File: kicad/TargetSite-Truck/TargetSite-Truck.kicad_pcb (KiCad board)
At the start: 2 copper layers, 75 x 50 mm, 11 parts, among them J2 HC05, M1 Motor_DC, U1 PIC16F1827-E/P, U2 TA7291P

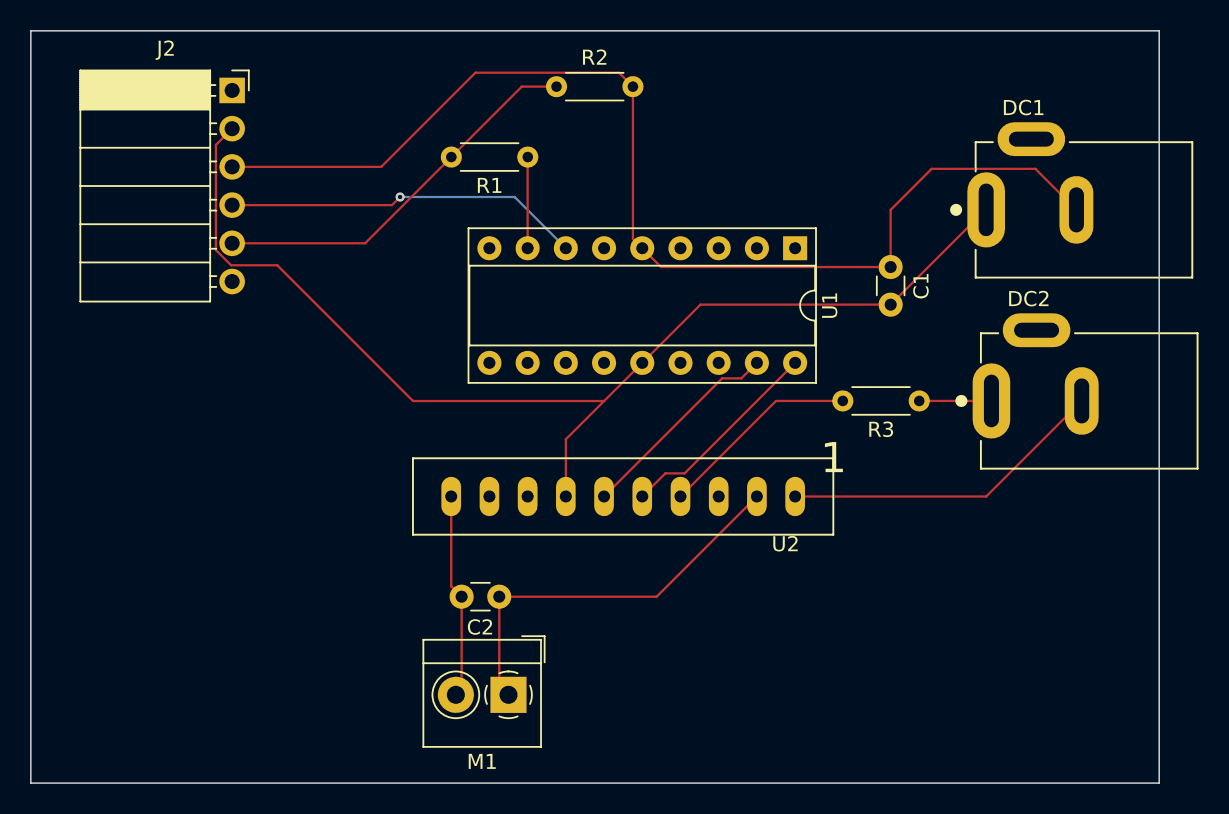
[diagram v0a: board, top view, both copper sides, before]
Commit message: 回路図の作成、PCBの作成
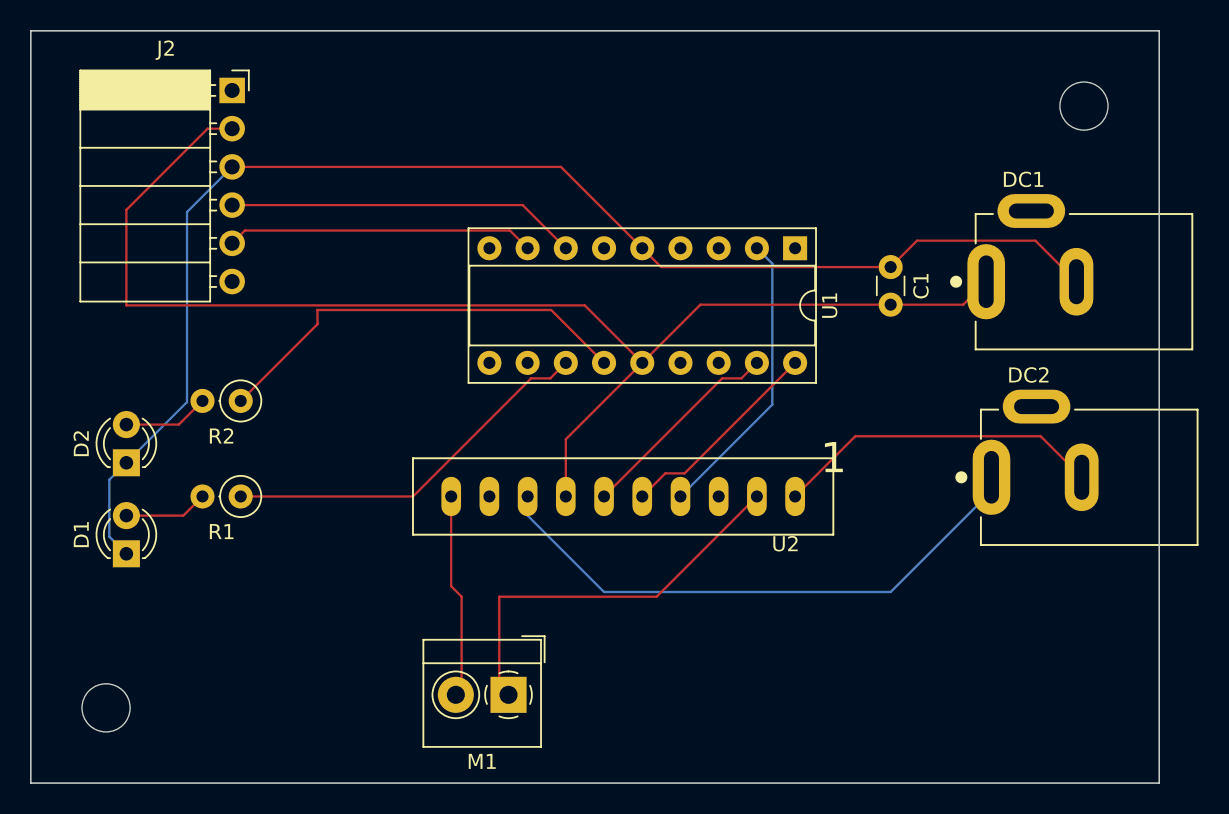
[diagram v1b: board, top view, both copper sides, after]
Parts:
- removed C2: 0.01u, Capacitor_THT:C_Disc_D3.0mm_W1.6mm_P2.50mm
- removed R3: 2.2k, Resistor_THT:R_Axial_DIN0204_L3.6mm_D1.6mm_P5.08mm_Horizontal
- added D1: LED_STATUS, LED_THT:LED_D3.0mm, F.Cu at (136.4, 114.8)
- added D2: LED_ACTIVATE, LED_THT:LED_D3.0mm, F.Cu at (136.4, 108.7)
- added MH1: MountingHole_3.2mm_M3, MountingHole:MountingHole_3.2mm_M3, F.Cu at (200.0, 85.0)
- added MH2: MountingHole_3.2mm_M3, MountingHole:MountingHole_3.2mm_M3, F.Cu at (135.0, 125.0)
- J2: value HC05 -> HM10
- R1: value 1k -> R330; footprint Resistor_THT:R_Axial_DIN0204_L3.6mm_D1.6mm_P5.08mm_Horizontal -> Resistor_THT:R_Axial_DIN0207_L6.3mm_D2.5mm_P2.54mm_Vertical
- R2: value 10k -> R330; footprint Resistor_THT:R_Axial_DIN0204_L3.6mm_D1.6mm_P5.08mm_Horizontal -> Resistor_THT:R_Axial_DIN0207_L6.3mm_D2.5mm_P2.54mm_Vertical
- moved R2 29.6 mm to (143.9, 104.6), turned to 180 degrees
- moved R1 29.5 mm to (143.9, 111.0)
- moved DC2 5.08 mm to (193.8, 109.7)
- moved DC1 4.77 mm to (193.5, 96.7)
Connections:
- net /DC_GND renamed DC_GND
- net /Driver_IN1 renamed Driver_IN1
- net /Driver_IN2 renamed Driver_IN2
- net /HC05_TX renamed HM10_TX
- net /Motor_IN1 renamed Motor_IN1
- net /Motor_IN2 renamed Motor_IN2
- DC2 pad 1: /DC_VCC -> DC_VCC
- J2 pad 5: /HC05_RX -> HM10_RX
- R1 pad 1: Net-(R1-Pad1) -> Net-(U1-Pad12)
- R1 pad 2: /HC05_RX -> Net-(D1-Pad2)
- R2 pad 1: /HC05_RX -> Net-(U1-Pad13)
- R2 pad 2: GND -> Net-(D2-Pad2)
- U1 pad 12: unconnected-(U1-Pad12) -> Net-(U1-Pad12)
- U1 pad 13: unconnected-(U1-Pad13) -> Net-(U1-Pad13)
- U1 pad 2: unconnected-(U1-Pad2) -> Driver_Ref
- U1 pad 8: Net-(R1-Pad1) -> HM10_RX
- U2 pad 4: /DC_VCC -> Driver_Ref
- U2 pad 8: /DC_VCC -> DC_VCC
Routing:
- net DC_VCC: track 0.00 -> 37.9 mm
- net Net-(U1-Pad13): track 0.00 -> 28.7 mm
- net /HC05_RX: track 25.9 -> 0.00 mm
- net Net-(U1-Pad12): track 0.00 -> 25.3 mm
- net HM10_RX: track 0.00 -> 20.5 mm
- net Driver_Ref: track 0.00 -> 19.5 mm
- net /DC_VCC: track 18.2 -> 0.00 mm
- net GND: track 76.1 -> 90.3 mm
- net VCC: track 76.5 -> 87.6 mm
- net Net-(R1-Pad1): track 6.06 -> 0.00 mm
- net Net-(D2-Pad2): track 0.00 -> 5.71 mm
- net Net-(D1-Pad2): track 0.00 -> 5.59 mm
- net HM10_TX: track 23.8 -> 23.4 mm, vias 1 -> 0

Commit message: ガーバーデータの作成
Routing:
- net GND: vias 0 -> 36
- added copper zone on B.Cu, net GND
- added copper zone on F.Cu, net GND
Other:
- board text added: "5V"
- board text added: "9V"
- board text added: "ACTIVE"
- board text added: "DC Motor"
- board text added: "GND"
- board text added: "HM-10 Pin Socket"
- board text added: "PIC16F1827"
- board text added: "RX"
- board text added: "STATUS"
- board text added: "TA7291P"
- board text added: "TX"
- board text added: "TargetSite-Front Dev:1 GTech9971 2023/05/27"
- board text added: "VCC"
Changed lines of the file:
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@@
     (grid_origin 130 130)
     (pcbplotparams
-      (layerselection 0x00010fc_ffffffff)
+      (layerselection 0x00010f0_ffffffff)
       (disableapertmacros false)
-      (usegerberextensions false)
-      (usegerberattributes true)
-      (usegerberadvancedattributes true)
-      (creategerberjobfile true)
+      (usegerberextensions true)
+      (usegerberattributes false)
+      (usegerberadvancedattributes false)
+      (creategerberjobfile false)
       (svguseinch false)
       (svgprecision 6)
       (excludeedgelayer true)
       (plotframeref false)
-      (viasonmask false)
+      (viasonmask true)
       (mode 1)
-      (useauxorigin false)
+      (useauxorigin true)
       (hpglpennumber 1)
       (hpglpenspeed 20)
@@
       (psa4output false)
       (plotreference true)
-      (plotvalue true)
+      (plotvalue false)
       (plotinvisibletext false)
       (sketchpadsonfab false)
@@
       (outputformat 1)
       (mirror false)
-      (drillshape 1)
+      (drillshape 0)
       (scaleselection 1)
       (outputdirectory "")
@@
   )
   (gr_rect locked (start 130 130) (end 205 80) (layer "Edge.Cuts") (width 0.1) (fill none))
+  (gr_text "RX" (at 145.875 94.44) (layer "F.SilkS")
+    (effects (font (size 1 1) (thickness 0.15)))
+  )
+  (gr_text "9V" (at 190.325 109.68 90) (layer "F.SilkS")
+    (effects (font (size 1 1) (thickness 0.15)))
+  )
+  (gr_text "GND" (at 145.875 89.36) (layer "F.SilkS")
+    (effects (font (size 1 1) (thickness 0.15)))
+  )
+  (gr_text "PIC16F1827" (at 184.61 98.25 90) (layer "F.SilkS")
+    (effects (font (size 1 1) (thickness 0.15)))
+  )
+  (gr_text "TargetSite-Front Dev:1\nGTech9971 2023/05/27" (at 185.245 126.825) (layer "F.SilkS")
+    (effects (font (size 1 1) (thickness 0.15)) (justify left))
+  )
+  (gr_text "VCC" (at 145.875 86.82) (layer "F.SilkS")
+    (effects (font (size 1 1) (thickness 0.15)))
+  )
+  (gr_text "TA7291P" (at 185.245 110.95 90) (layer "F.SilkS")
+    (effects (font (size 1 1) (thickness 0.15)))
+  )
+  (gr_text "ACTIVE" (at 131.905 107.14 90) (layer "F.SilkS")
+    (effects (font (size 1 1) (thickness 0.15)))
+  )
+  (gr_text "STATUS" (at 131.905 113.49 90) (layer "F.SilkS")
+    (effects (font (size 1 1) (thickness 0.15)))
+  )
+  (gr_text "DC Motor" (at 159.845 118.57) (layer "F.SilkS")
+    (effects (font (size 1 1) (thickness 0.15)))
+  )
+  (gr_text "TX" (at 145.875 91.9) (layer "F.SilkS")
+    (effects (font (size 1 1) (thickness 0.15)))
+  )
+  (gr_text "HM-10 Pin Socket" (at 138.89 99.52) (layer "F.SilkS")
+    (effects (font (size 1 1) (thickness 0.15)))
+  )
+  (gr_text "5V" (at 190.96 96.98 90) (layer "F.SilkS")
+    (effects (font (size 1 1) (thickness 0.15)))
+  )
   (segment (start 136.35 91.9) (end 136.35 98.25) (width 0.1524) (layer "F.Cu") (net 1))
   (segment (start 191.975 98.2) (end 193.5 96.675) (width 0.1524) (layer "F.Cu") (net 1))
   (segment (start 166.82 98.25) (end 170.64 102.07) (width 0.1524) (layer "F.Cu") (net 1))
-  (segment (start 165.56 107.15) (end 168.105 104.605) (width 0.1524) (layer "F.Cu") (net 1))
+  (segment (start 165.56 107.15) (end 170.64 102.07) (width 0.1524) (layer "F.Cu") (net 1))
   (segment (start 141.74715 86.50285) (end 136.35 91.9) (width 0.1524) (layer "F.Cu") (net 1))
   (segment (start 187.15 98.2) (end 191.975 98.2) (width 0.1524) (layer "F.Cu") (net 1))
-  (segment (start 168.105 104.605) (end 170.64 102.07) (width 0.1524) (layer "F.Cu") (net 1))
   (segment (start 143.38 86.50285) (end 141.74715 86.50285) (width 0.1524) (layer "F.Cu") (net 1))
   (segment (start 187.15 98.2) (end 174.51 98.2) (width 0.1524) (layer "F.Cu") (net 1))
@@
   (segment (start 170.64 94.45) (end 165.23285 89.04285) (width 0.1524) (layer "F.Cu") (net 2))
   (segment (start 196.7714 93.9464) (end 199.5 96.675) (width 0.1524) (layer "F.Cu") (net 2))
+  (via (at 150.32 84.28) (size 0.605) (drill 0.3) (layers "F.Cu" "B.Cu") (free) (net 2))
+  (via (at 194.77 124.285) (size 0.605) (drill 0.3) (layers "F.Cu" "B.Cu") (free) (net 2))
+  (via (at 183.975 119.205) (size 0.605) (drill 0.3) (layers "F.Cu" "B.Cu") (free) (net 2))
+  (via (at 149.05 119.205) (size 0.605) (drill 0.3) (layers "F.Cu" "B.Cu") (free) (net 2))
+  (via (at 157.305 103.965) (size 0.605) (drill 0.3) (layers "F.Cu" "B.Cu") (free) (net 2))
+  (via (at 144.605 119.205) (size 0.605) (drill 0.3) (layers "F.Cu" "B.Cu") (free) (net 2))
+  (via (at 190.96 90.63) (size 0.605) (drill 0.3) (layers "F.Cu" "B.Cu") (free) (net 2))
+  (via (at 166.195 119.205) (size 0.605) (drill 0.3) (layers "F.Cu" "B.Cu") (free) (net 2))
+  (via (at 150.32 89.995) (size 0.605) (drill 0.3) (layers "F.Cu" "B.Cu") (free) (net 2))
+  (via (at 150.32 96.345) (size 0.605) (drill 0.3) (layers "F.Cu" "B.Cu") (free) (net 2))
+  (via (at 153.495 124.285) (size 0.605) (drill 0.3) (layers "F.Cu" "B.Cu") (free) (net 2))
+  (via (at 150.32 103.965) (size 0.605) (drill 0.3) (layers "F.Cu" "B.Cu") (free) (net 2))
+  (via (at 181.435 104.6) (size 0.605) (drill 0.3) (layers "F.Cu" "B.Cu") (free) (net 2))
+  (via (at 168.735 107.14) (size 0.605) (drill 0.3) (layers "F.Cu" "B.Cu") (free) (net 2))
+  (via (at 183.975 124.285) (size 0.605) (drill 0.3) (layers "F.Cu" "B.Cu") (free) (net 2))
+  (via (at 175.085 124.285) (size 0.605) (drill 0.3) (layers "F.Cu" "B.Cu") (free) (net 2))
+  (via (at 164.925 90.63) (size 0.605) (drill 0.3) (layers "F.Cu" "B.Cu") (free) (net 2))
+  (via (at 149.05 124.285) (size 0.605) (drill 0.3) (layers "F.Cu" "B.Cu") (free) (net 2))
+  (via (at 164.925 104.6) (size 0.605) (drill 0.3) (layers "F.Cu" "B.Cu") (free) (net 2))
+  (via (at 194.77 119.205) (size 0.605) (drill 0.3) (layers "F.Cu" "B.Cu") (free) (net 2))
+  (via (at 190.96 104.6) (size 0.605) (drill 0.3) (layers "F.Cu" "B.Cu") (free) (net 2))
+  (via (at 166.195 124.285) (size 0.605) (drill 0.3) (layers "F.Cu" "B.Cu") (free) (net 2))
+  (via (at 164.925 84.28) (size 0.605) (drill 0.3) (layers "F.Cu" "B.Cu") (free) (net 2))
+  (via (at 178.26 90.63) (size 0.605) (drill 0.3) (layers "F.Cu" "B.Cu") (free) (net 2))
+  (via (at 157.305 96.345) (size 0.605) (drill 0.3) (layers "F.Cu" "B.Cu") (free) (net 2))
+  (via (at 177.625 96.345) (size 0.605) (drill 0.3) (layers "F.Cu" "B.Cu") (free) (net 2))
+  (via (at 178.26 84.28) (size 0.605) (drill 0.3) (layers "F.Cu" "B.Cu") (free) (net 2))
+  (via (at 175.085 119.205) (size 0.605) (drill 0.3) (layers "F.Cu" "B.Cu") (free) (net 2))
+  (via (at 136.35 103.965) (size 0.605) (drill 0.3) (layers "F.Cu" "B.Cu") (free) (net 2))
+  (via (at 136.35 119.205) (size 0.605) (drill 0.3) (layers "F.Cu" "B.Cu") (free) (net 2))
+  (via (at 162.385 107.14) (size 0.605) (drill 0.3) (layers "F.Cu" "B.Cu") (free) (net 2))
+  (via (at 171.91 104.6) (size 0.605) (drill 0.3) (layers "F.Cu" "B.Cu") (free) (net 2))
+  (via (at 161.75 96.345) (size 0.605) (drill 0.3) (layers "F.Cu" "B.Cu") (free) (net 2))
+  (via (at 144.605 124.285) (size 0.605) (drill 0.3) (layers "F.Cu" "B.Cu") (free) (net 2))
+  (via (at 153.495 119.205) (size 0.605) (drill 0.3) (layers "F.Cu" "B.Cu") (free) (net 2))
+  (via (at 190.96 84.28) (size 0.605) (drill 0.3) (layers "F.Cu" "B.Cu") (free) (net 2))
   (segment (start 136.350452 108.71) (end 135.221852 109.8386) (width 0.1524) (layer "B.Cu") (net 2))
   (segment (start 135.221852 113.6314) (end 136.350452 114.76) (width 0.1524) (layer "B.Cu") (net 2))
@@
   (segment (start 168.1 102.07) (end 164.5848 98.5548) (width 0.1524) (layer "F.Cu") (net 28))
   (segment (start 164.5848 98.5548) (end 149.05 98.5548) (width 0.1524) (layer "F.Cu") (net 28))
+  (zone (net 2) (net_name "GND") (layers F&B.Cu) (hatch edge 0.508)
+    (connect_pads (clearance 0.35))
+    (min_thickness 0.254) (filled_areas_thickness no)
+    (fill yes (thermal_gap 0.508) (thermal_bridge_width 0.508))
+    (polygon
+      (pts
+        (xy 204.5 129.5)
+        (xy 130.5 129.5)
+        (xy 130.5 80.5)
+        (xy 204.5 80.5)
+      )
+    )
+  )
 )

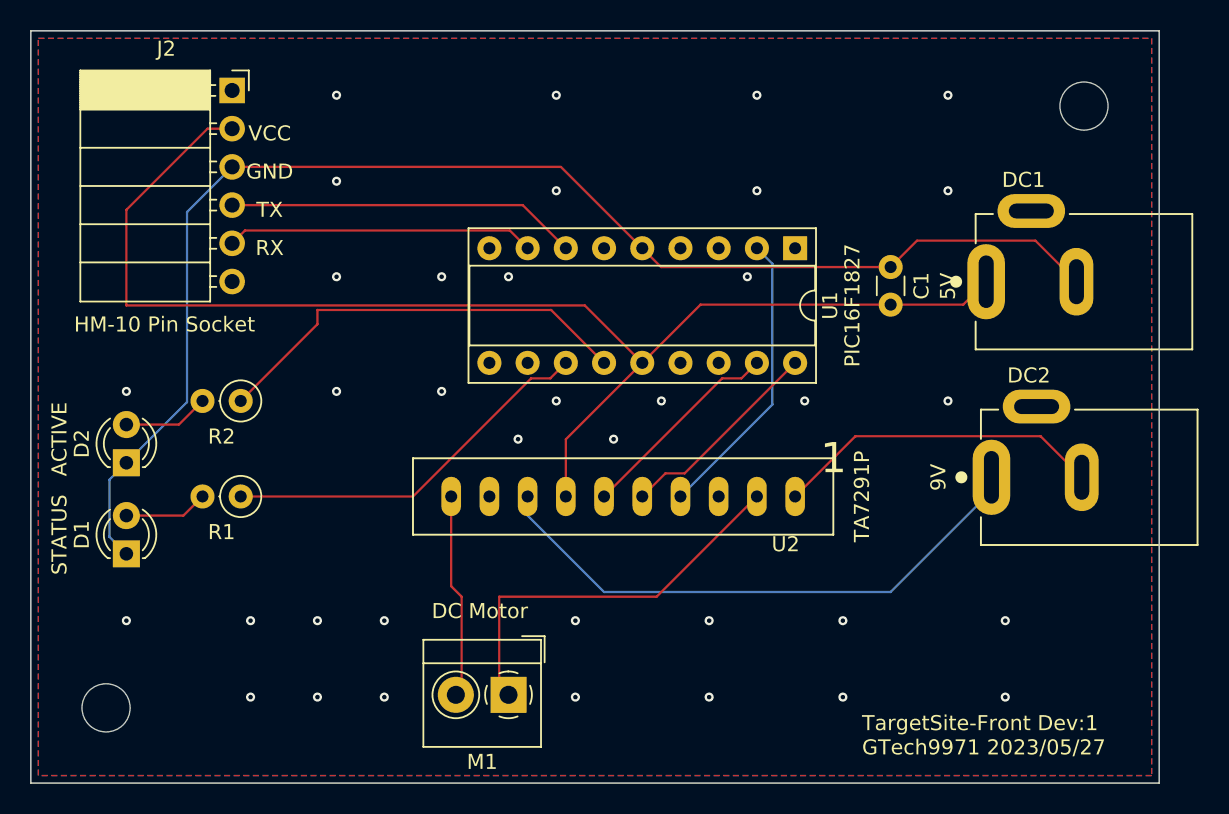
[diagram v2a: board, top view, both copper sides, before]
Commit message: 回路基板設計修正
RA0、RA1の配線を引き直した
ターミナルのピッチサイズを5.08mmに変更
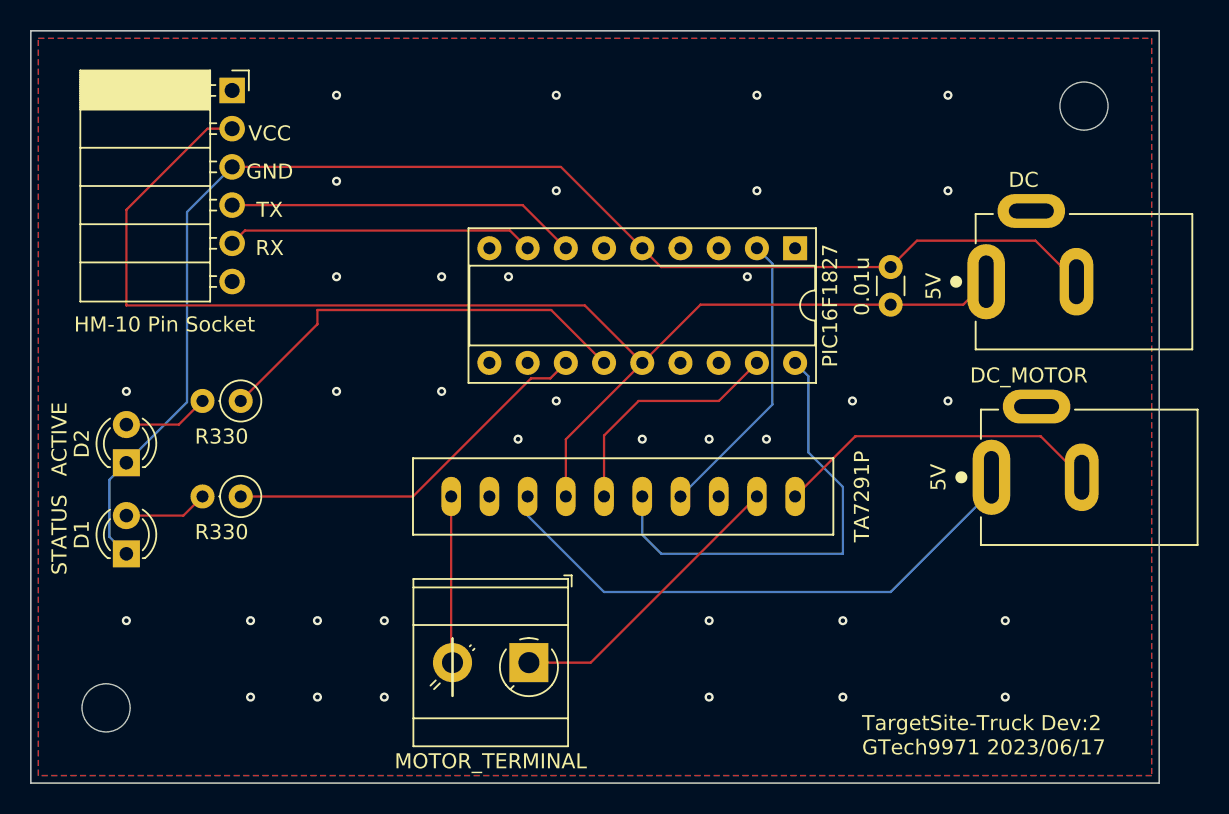
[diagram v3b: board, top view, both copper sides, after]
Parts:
- HM-10 Pin Socket: renamed from J2
- MOTOR_TERMINAL: renamed from M1; footprint TerminalBlock_4Ucon:TerminalBlock_4Ucon_1x02_P3.50mm_Horizontal -> TerminalBlock_MetzConnect:TerminalBlock_MetzConnect_Type073_RT02602HBLU_1x02_P5.08mm_Horizontal
- moved MOTOR_TERMINAL 2.53 mm to (163.1, 122.0)
- renumbered C1 to 0.01u, DC1 to DC, DC2 to DC_MOTOR, U1 to PIC16F1827, R1 to R330, R2 to R330, U2 to TA7291P
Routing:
- net Driver_IN1: track 13.8 -> 30.4 mm
- net Motor_IN1: track 26.7 -> 19.7 mm
- net Motor_IN2: track 13.6 -> 11.1 mm
- net Driver_IN2: track 13.8 -> 16.2 mm
- net GND: vias 36 -> 35
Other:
- board text added: "NC"
- board text added: "TargetSite-Truck Dev:2 GTech9971 2023/06/17"
- board text removed: "9V"
- board text removed: "DC Motor"
- board text removed: "HM-10 Pin Socket"
- board text removed: "PIC16F1827"
- board text removed: "TA7291P"
- board text removed: "TargetSite-Front Dev:1 GTech9971 2023/05/27"
